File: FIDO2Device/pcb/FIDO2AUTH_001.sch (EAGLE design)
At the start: 19 parts, among them CN1 TE-1734028, SW1 SKRPACE010, U1 MDBT50Q-P1M, X1 NX3215SA-32.768K

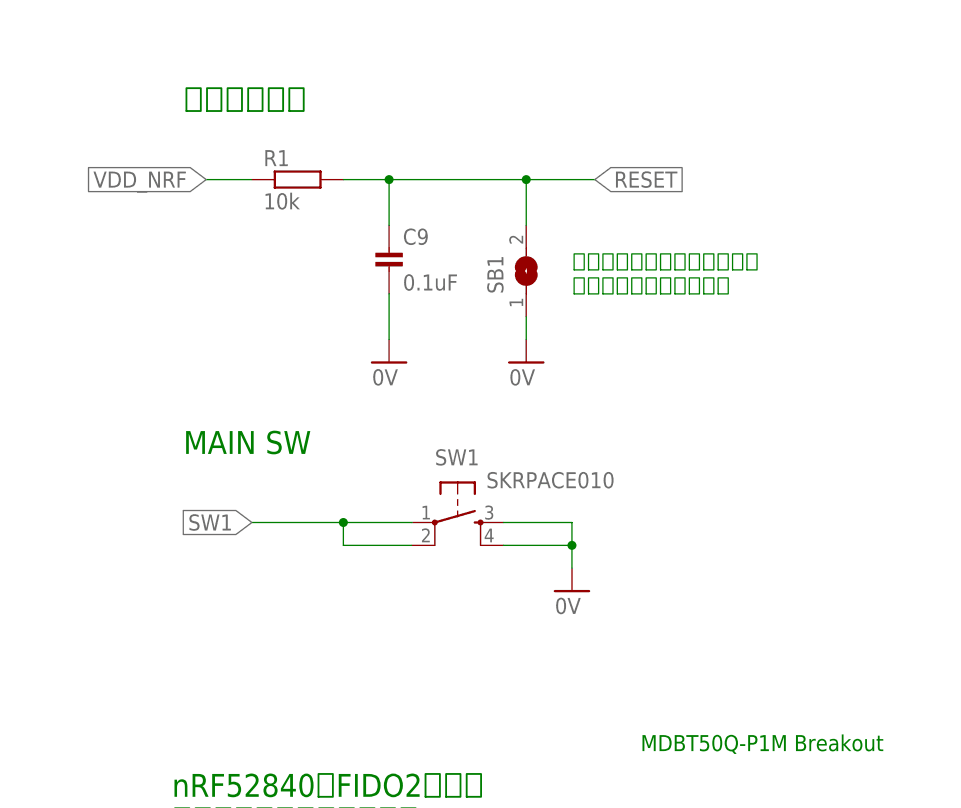
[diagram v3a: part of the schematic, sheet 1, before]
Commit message: [WIP] ブレークアウト基板回路図
・リセット回路を、ジャンパーではなく超小型タクトスイッチに置換え
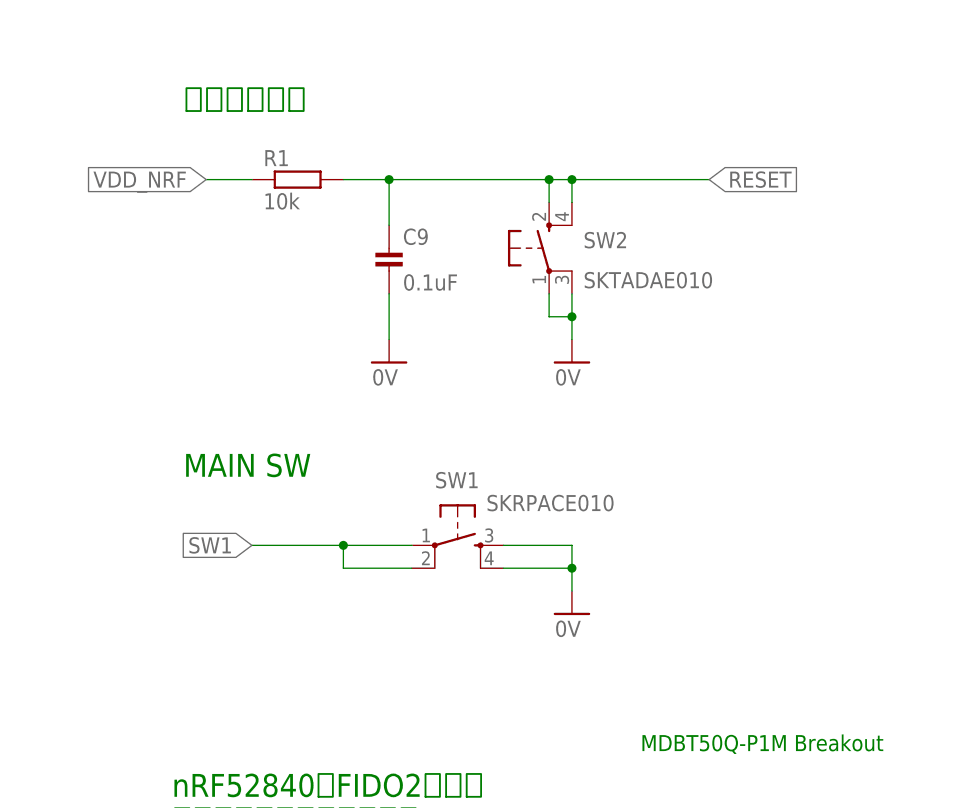
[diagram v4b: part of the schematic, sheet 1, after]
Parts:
- removed SB1: (no value), Connectors:SJ
- added SW2: SKTADAE010, Parts:SKTADAE010
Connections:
- net 0V: now also SW2.P, SW2.P1; no longer SB1.1
- net RESET: now also SW2.S, SW2.S1; no longer SB1.2
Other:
- note removed: "ジャンパーをショートすると リセットがかかります。"
- moved on the sheet: SW1
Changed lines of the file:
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@@
 <setting verticaltext="up"/>
 </settings>
-<grid distance="0.1" unitdist="inch" unit="inch" style="lines" multiple="1" display="yes" altdistance="0.01" altunitdist="inch" altunit="inch"/>
+<grid distance="0.1" unitdist="inch" unit="inch" style="lines" multiple="1" display="no" altdistance="0.01" altunitdist="inch" altunit="inch"/>
 <layers>
 <layer number="1" name="Top" color="4" fill="1" visible="no" active="no"/>
@@
 <part name="C9" library="Parts" deviceset="CAP" device="_0402" value="0.1uF"/>
 <part name="GND11" library="Supply" deviceset="0V" device=""/>
-<part name="SB1" library="Connectors" deviceset="SJ" device=""/>
-<part name="GND12" library="Supply" deviceset="0V" device=""/>
 <part name="SW1" library="Parts" deviceset="SKRPACE010" device=""/>
 <part name="GND13" library="Supply" deviceset="0V" device=""/>
+<part name="SW2" library="Parts" deviceset="SKTADAE010" device=""/>
+<part name="GND12" library="Supply" deviceset="0V" device=""/>
 </parts>
 <sheets>
@@
 <text x="20.32" y="162.56" size="3.81" layer="91">モジュール部</text>
 <text x="167.64" y="91.44" size="2.54" layer="91">リセット回路</text>
-<text x="210.82" y="71.12" size="1.778" layer="91">ジャンパーをショートすると
-リセットがかかります。</text>
-<text x="167.64" y="53.34" size="2.54" layer="91">MAIN SW</text>
+<text x="167.64" y="50.8" size="2.54" layer="91">MAIN SW</text>
 </plain>
 <instances>
@@
 <instance part="C9" gate="G$1" x="190.5" y="78.74"/>
 <instance part="GND11" gate="1" x="190.5" y="63.5"/>
-<instance part="SB1" gate="1" x="205.74" y="73.66" rot="R90"/>
-<instance part="GND12" gate="1" x="205.74" y="63.5"/>
-<instance part="SW1" gate="G$1" x="198.12" y="45.72" rot="R270"/>
-<instance part="GND13" gate="1" x="210.82" y="38.1"/>
+<instance part="SW1" gate="G$1" x="198.12" y="43.18" rot="R270"/>
+<instance part="GND13" gate="1" x="210.82" y="35.56"/>
+<instance part="SW2" gate="G$1" x="208.28" y="76.2" smashed="yes">
+<attribute name="NAME" x="212.09" y="76.2" size="1.778" layer="95"/>
+<attribute name="VALUE" x="212.09" y="71.755" size="1.778" layer="96"/>
+</instance>
+<instance part="GND12" gate="1" x="210.82" y="63.5"/>
 </instances>
 <busses>
@@
 </segment>
 <segment>
-<pinref part="SB1" gate="1" pin="1"/>
+<pinref part="SW1" gate="G$1" pin="S"/>
+<wire x1="203.2" y1="43.18" x2="210.82" y2="43.18" width="0.1524" layer="91"/>
+<pinref part="GND13" gate="1" pin="0V"/>
+<wire x1="210.82" y1="43.18" x2="210.82" y2="40.64" width="0.1524" layer="91"/>
+<pinref part="SW1" gate="G$1" pin="S1"/>
+<wire x1="210.82" y1="40.64" x2="210.82" y2="38.1" width="0.1524" layer="91"/>
+<wire x1="203.2" y1="40.64" x2="210.82" y2="40.64" width="0.1524" layer="91"/>
+<junction x="210.82" y="40.64"/>
+</segment>
+<segment>
 <pinref part="GND12" gate="1" pin="0V"/>
-<wire x1="205.74" y1="68.58" x2="205.74" y2="66.04" width="0.1524" layer="91"/>
-</segment>
-<segment>
-<pinref part="SW1" gate="G$1" pin="S"/>
-<wire x1="203.2" y1="45.72" x2="210.82" y2="45.72" width="0.1524" layer="91"/>
-<pinref part="GND13" gate="1" pin="0V"/>
-<wire x1="210.82" y1="45.72" x2="210.82" y2="43.18" width="0.1524" layer="91"/>
-<pinref part="SW1" gate="G$1" pin="S1"/>
-<wire x1="210.82" y1="43.18" x2="210.82" y2="40.64" width="0.1524" layer="91"/>
-<wire x1="203.2" y1="43.18" x2="210.82" y2="43.18" width="0.1524" layer="91"/>
-<junction x="210.82" y="43.18"/>
+<pinref part="SW2" gate="G$1" pin="P1"/>
+<wire x1="210.82" y1="66.04" x2="210.82" y2="68.58" width="0.1524" layer="91"/>
+<pinref part="SW2" gate="G$1" pin="P"/>
+<wire x1="210.82" y1="68.58" x2="210.82" y2="71.12" width="0.1524" layer="91"/>
+<wire x1="208.28" y1="71.12" x2="208.28" y2="68.58" width="0.1524" layer="91"/>
+<wire x1="208.28" y1="68.58" x2="210.82" y2="68.58" width="0.1524" layer="91"/>
+<junction x="210.82" y="68.58"/>
 </segment>
 </net>
@@
 <wire x1="185.42" y1="83.82" x2="190.5" y2="83.82" width="0.1524" layer="91"/>
 <wire x1="190.5" y1="83.82" x2="190.5" y2="78.74" width="0.1524" layer="91"/>
-<wire x1="190.5" y1="83.82" x2="205.74" y2="83.82" width="0.1524" layer="91"/>
 <junction x="190.5" y="83.82"/>
-<label x="213.36" y="83.82" size="1.778" layer="95" xref="yes"/>
-<pinref part="SB1" gate="1" pin="2"/>
-<wire x1="205.74" y1="83.82" x2="213.36" y2="83.82" width="0.1524" layer="91"/>
-<wire x1="205.74" y1="78.74" x2="205.74" y2="83.82" width="0.1524" layer="91"/>
-<junction x="205.74" y="83.82"/>
+<label x="226.06" y="83.82" size="1.778" layer="95" xref="yes"/>
+<wire x1="190.5" y1="83.82" x2="208.28" y2="83.82" width="0.1524" layer="91"/>
+<pinref part="SW2" gate="G$1" pin="S"/>
+<wire x1="208.28" y1="83.82" x2="210.82" y2="83.82" width="0.1524" layer="91"/>
+<wire x1="210.82" y1="83.82" x2="226.06" y2="83.82" width="0.1524" layer="91"/>
+<wire x1="208.28" y1="81.28" x2="208.28" y2="83.82" width="0.1524" layer="91"/>
+<junction x="208.28" y="83.82"/>
+<pinref part="SW2" gate="G$1" pin="S1"/>
+<wire x1="210.82" y1="81.28" x2="210.82" y2="83.82" width="0.1524" layer="91"/>
+<junction x="210.82" y="83.82"/>
 </segment>
 </net>
@@
 <segment>
 <pinref part="SW1" gate="G$1" pin="P"/>
-<wire x1="193.04" y1="45.72" x2="185.42" y2="45.72" width="0.1524" layer="91"/>
-<label x="175.26" y="45.72" size="1.778" layer="95" rot="R180" xref="yes"/>
+<wire x1="193.04" y1="43.18" x2="185.42" y2="43.18" width="0.1524" layer="91"/>
+<label x="175.26" y="43.18" size="1.778" layer="95" rot="R180" xref="yes"/>
 <pinref part="SW1" gate="G$1" pin="P1"/>
-<wire x1="185.42" y1="45.72" x2="175.26" y2="45.72" width="0.1524" layer="91"/>
-<wire x1="193.04" y1="43.18" x2="185.42" y2="43.18" width="0.1524" layer="91"/>
-<wire x1="185.42" y1="43.18" x2="185.42" y2="45.72" width="0.1524" layer="91"/>
-<junction x="185.42" y="45.72"/>
-</segment>
-</net>
+<wire x1="185.42" y1="43.18" x2="175.26" y2="43.18" width="0.1524" layer="91"/>
+<wire x1="193.04" y1="40.64" x2="185.42" y2="40.64" width="0.1524" layer="91"/>
+<wire x1="185.42" y1="40.64" x2="185.42" y2="43.18" width="0.1524" layer="91"/>
+<junction x="185.42" y="43.18"/>
+</segment>
+</net>

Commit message: [WIP] ブレークアウト基板回路図
・LED２点配置
・リセットスイッチ配置
・各部品の配置を見直し
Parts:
- added LED1: APHD1608LSURCK, Parts:APHD1608LSURCK
- added LED2: APHF1608LSEEQBDZGKC, Parts:APHF1608LSEEQBDZGKC
- added R2: 1.5k, Parts:RESISTOR_0402
- added R3: 1.2k, Parts:RESISTOR_0402
- added R4: 2.2k, Parts:RESISTOR_0402
- added R5: 390, Parts:RESISTOR_0402
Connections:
- net N$1 renamed VBUS
- removed net NFC1: U1.P0.09/NFC1
- removed net NFC2: U1.P0.10/NFC2
- new net N$10: LED2.CGREEN, R5.2
- new net N$11: LED1.C, R2.2
- new net N$8: LED2.CRED, R3.2
- new net N$9: LED2.CBLUE, R4.2
- net LED1: now also R2.1
- net LED2_B: now also R5.1
- net LED2_G: now also R4.1
- net LED2_R: now also R3.1
- net VDD_NRF: now also LED1.A, LED2.A
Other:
- note added: "LED部"
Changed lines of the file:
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@@
 <setting verticaltext="up"/>
 </settings>
-<grid distance="0.1" unitdist="inch" unit="inch" style="lines" multiple="1" display="no" altdistance="0.01" altunitdist="inch" altunit="inch"/>
+<grid distance="0.1" unitdist="inch" unit="inch" style="lines" multiple="1" display="yes" altdistance="0.01" altunitdist="inch" altunit="inch"/>
 <layers>
 <layer number="1" name="Top" color="4" fill="1" visible="no" active="no"/>
@@
 <part name="SW2" library="Parts" deviceset="SKTADAE010" device=""/>
 <part name="GND12" library="Supply" deviceset="0V" device=""/>
+<part name="LED1" library="Parts" deviceset="APHD1608" device="LSURCK"/>
+<part name="LED2" library="Parts" deviceset="APHF1608" device="LSEEQBDZGKC"/>
+<part name="R2" library="Parts" deviceset="RESISTOR" device="_0402" value="1.5k"/>
+<part name="R3" library="Parts" deviceset="RESISTOR" device="_0402" value="1.2k"/>
+<part name="R4" library="Parts" deviceset="RESISTOR" device="_0402" value="2.2k"/>
+<part name="R5" library="Parts" deviceset="RESISTOR" device="_0402" value="390"/>
 </parts>
 <sheets>
@@
 </segment>
 </net>
-<net name="NFC1" class="0">
-<segment>
-<pinref part="U1" gate="G$1" pin="P0.09/NFC1"/>
-<wire x1="104.14" y1="116.84" x2="116.84" y2="116.84" width="0.1524" layer="91"/>
-<label x="116.84" y="134.62" size="1.778" layer="95" rot="R90" xref="yes"/>
-<wire x1="116.84" y1="116.84" x2="116.84" y2="134.62" width="0.1524" layer="91"/>
-</segment>
-</net>
-<net name="NFC2" class="0">
-<segment>
-<pinref part="U1" gate="G$1" pin="P0.10/NFC2"/>
-<wire x1="104.14" y1="121.92" x2="111.76" y2="121.92" width="0.1524" layer="91"/>
-<wire x1="111.76" y1="121.92" x2="111.76" y2="134.62" width="0.1524" layer="91"/>
-<label x="111.76" y="134.62" size="1.778" layer="95" rot="R90" xref="yes"/>
-</segment>
-</net>
 <net name="SWDIO" class="0">
 <segment>
@@
 <text x="166.37" y="11.43" size="2.54" layer="91">nRF52840版FIDO2認証器
 開発用ブレークアウト基板</text>
+<text x="30.48" y="91.44" size="3.81" layer="91">LED部</text>
 </plain>
 <instances>
@@
 <instance part="D1" gate="G$1" x="114.3" y="124.46"/>
 <instance part="CN1" gate="G$1" x="30.48" y="124.46"/>
+<instance part="LED1" gate="G$1" x="55.88" y="60.96" smashed="yes">
+<attribute name="NAME" x="59.436" y="58.928" size="1.778" layer="95"/>
+<attribute name="VALUE" x="59.055" y="56.388" size="1.778" layer="96"/>
+</instance>
+<instance part="LED2" gate="G$1" x="96.52" y="60.96"/>
+<instance part="R2" gate="G$1" x="55.88" y="40.64" rot="R90"/>
+<instance part="R3" gate="G$1" x="86.36" y="40.64" rot="R90"/>
+<instance part="R4" gate="G$1" x="96.52" y="40.64" rot="R90"/>
+<instance part="R5" gate="G$1" x="106.68" y="40.64" rot="R90"/>
 </instances>
 <busses>
 </busses>
 <nets>
-<net name="N$1" class="0">
+<net name="VBUS" class="0">
 <segment>
 <wire x1="50.8" y1="137.16" x2="60.96" y2="137.16" width="0.1524" layer="91"/>
@@
 </segment>
 </net>
+<net name="VDD_NRF" class="0">
+<segment>
+<pinref part="LED1" gate="G$1" pin="A"/>
+<wire x1="55.88" y1="63.5" x2="55.88" y2="68.58" width="0.1524" layer="91"/>
+<label x="55.88" y="68.58" size="1.778" layer="95" rot="R90" xref="yes"/>
+</segment>
+<segment>
+<pinref part="LED2" gate="G$1" pin="A"/>
+<wire x1="91.44" y1="63.5" x2="91.44" y2="68.58" width="0.1524" layer="91"/>
+<label x="91.44" y="68.58" size="1.778" layer="95" rot="R90" xref="yes"/>
+</segment>
+</net>
+<net name="LED1" class="0">
+<segment>
+<pinref part="R2" gate="G$1" pin="1"/>
+<wire x1="55.88" y1="40.64" x2="55.88" y2="35.56" width="0.1524" layer="91"/>
+<label x="55.88" y="35.56" size="1.778" layer="95" rot="R270" xref="yes"/>
+</segment>
+</net>
+<net name="LED2_R" class="0">
+<segment>
+<pinref part="R3" gate="G$1" pin="1"/>
+<wire x1="86.36" y1="40.64" x2="86.36" y2="35.56" width="0.1524" layer="91"/>
+<label x="86.36" y="35.56" size="1.778" layer="95" rot="R270" xref="yes"/>
+</segment>
+</net>
+<net name="LED2_G" class="0">
+<segment>
+<pinref part="R4" gate="G$1" pin="1"/>
+<wire x1="96.52" y1="40.64" x2="96.52" y2="35.56" width="0.1524" layer="91"/>
+<label x="96.52" y="35.56" size="1.778" layer="95" rot="R270" xref="yes"/>
+</segment>
+</net>
+<net name="LED2_B" class="0">
+<segment>
+<pinref part="R5" gate="G$1" pin="1"/>
+<wire x1="106.68" y1="40.64" x2="106.68" y2="35.56" width="0.1524" layer="91"/>
+<label x="106.68" y="35.56" size="1.778" layer="95" rot="R270" xref="yes"/>
+</segment>
+</net>
+<net name="N$8" class="0">
+<segment>
+<pinref part="LED2" gate="G$1" pin="CRED"/>
+<wire x1="91.44" y1="55.88" x2="91.44" y2="53.34" width="0.1524" layer="91"/>
+<wire x1="91.44" y1="53.34" x2="86.36" y2="53.34" width="0.1524" layer="91"/>
+<pinref part="R3" gate="G$1" pin="2"/>
+<wire x1="86.36" y1="53.34" x2="86.36" y2="50.8" width="0.1524" layer="91"/>
+</segment>
+</net>
+<net name="N$9" class="0">
+<segment>
+<pinref part="LED2" gate="G$1" pin="CBLUE"/>
+<pinref part="R4" gate="G$1" pin="2"/>
+<wire x1="96.52" y1="55.88" x2="96.52" y2="50.8" width="0.1524" layer="91"/>
+</segment>
+</net>
+<net name="N$10" class="0">
+<segment>
+<pinref part="LED2" gate="G$1" pin="CGREEN"/>
+<wire x1="101.6" y1="55.88" x2="101.6" y2="53.34" width="0.1524" layer="91"/>
+<wire x1="101.6" y1="53.34" x2="106.68" y2="53.34" width="0.1524" layer="91"/>
+<pinref part="R5" gate="G$1" pin="2"/>
+<wire x1="106.68" y1="53.34" x2="106.68" y2="50.8" width="0.1524" layer="91"/>
+</segment>
+</net>
+<net name="N$11" class="0">
+<segment>
+<pinref part="LED1" gate="G$1" pin="C"/>
+<pinref part="R2" gate="G$1" pin="2"/>
+<wire x1="55.88" y1="55.88" x2="55.88" y2="50.8" width="0.1524" layer="91"/>
+</segment>
+</net>
